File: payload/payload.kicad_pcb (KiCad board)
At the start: 2 copper layers, 90.2 x 95.9 mm, 49 parts, among them IC301 PIC16F1503-I_SL, J101 Conn_02x26_Odd_Even, J102 Conn_02x26_Odd_Even, J301 TC2030-MCP-NL-10, J401 Conn_01x06_Female, J501 Conn_01x02, J502 AVR-ISP-6, U101 PCA9548APW, U401 STM32F103C8T6, U501 ATmega328-P, Y401 8MHz, Y501 ECS-100-S-20A-TR

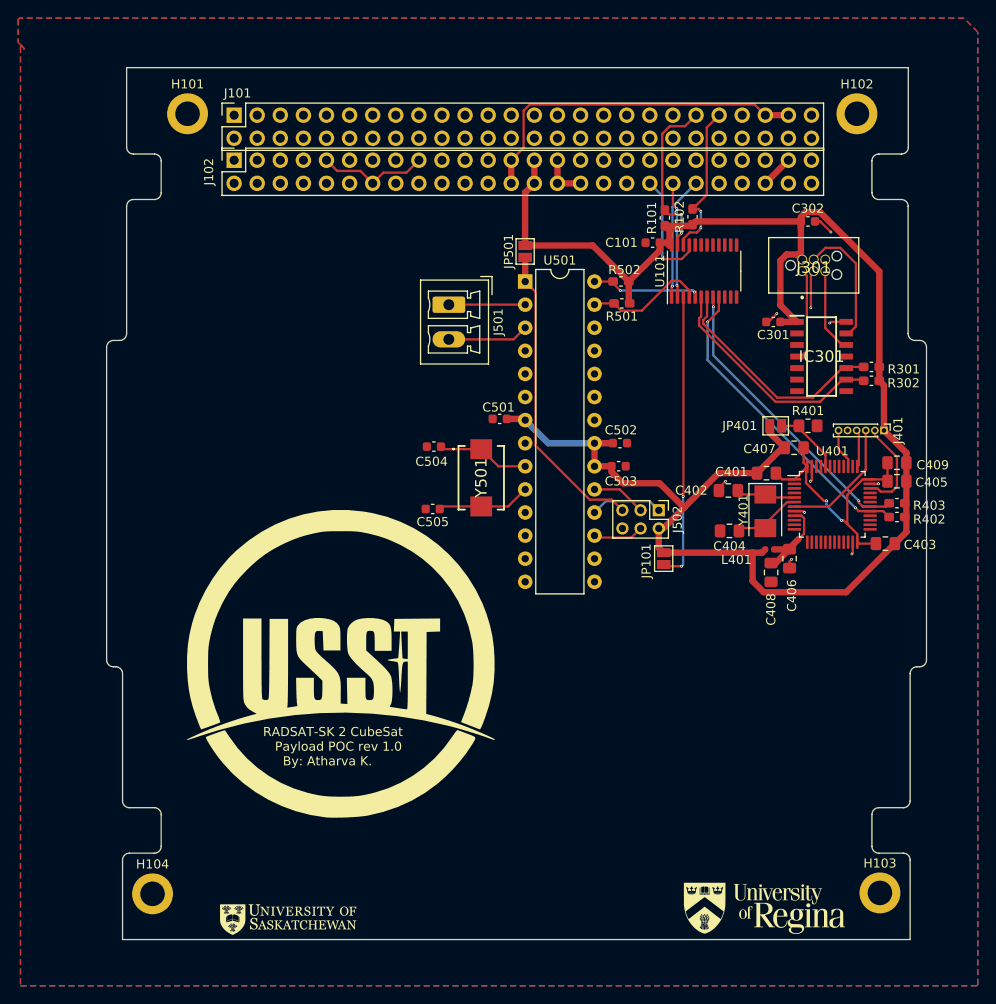
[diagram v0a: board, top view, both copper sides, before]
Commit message: added LEDs
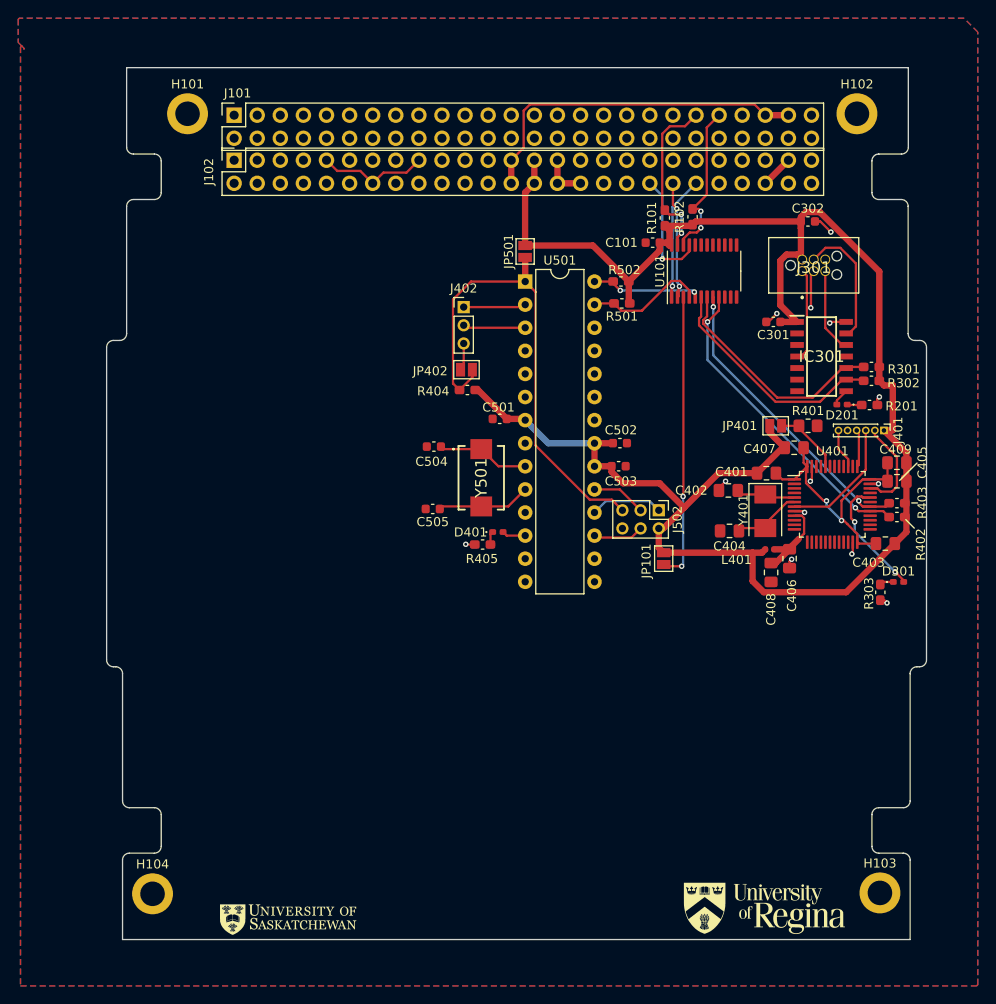
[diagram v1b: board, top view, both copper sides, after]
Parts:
- removed J501: Conn_01x02, Connector_Phoenix_MC:PhoenixContact_MCV_1,5_2-G-3.81_1x02_P3.81mm_Vertical
- added D201: LED, LED_SMD:LED_0402_1005Metric_Pad0.77x0.64mm_HandSolder, F.Cu at (178.1, 85.3)
- added D301: LED, LED_SMD:LED_0402_1005Metric_Pad0.77x0.64mm_HandSolder, F.Cu at (184.3, 104.8)
- added D401: LED, LED_SMD:LED_0402_1005Metric_Pad0.77x0.64mm_HandSolder, F.Cu at (140.3, 99.3)
- added J402: Conn_01x03, Connector_PinHeader_2.00mm:PinHeader_1x03_P2.00mm_Vertical, F.Cu at (136.5, 74.6)
- added JP402: Jumper_2_Open, Jumper:SolderJumper-2_P1.3mm_Open_Pad1.0x1.5mm, F.Cu at (136.8, 81.5)
- added R201: 1k, Capacitor_SMD:C_0603_1608Metric_Pad1.08x0.95mm_HandSolder, F.Cu at (181.1, 85.3)
- added R303: 1k, Capacitor_SMD:C_0603_1608Metric_Pad1.08x0.95mm_HandSolder, F.Cu at (182.3, 105.9)
- added R404: 2k, Capacitor_SMD:C_0603_1608Metric_Pad1.08x0.95mm_HandSolder, F.Cu at (136.9, 83.7)
- added R405: 1k, Capacitor_SMD:C_0603_1608Metric_Pad1.08x0.95mm_HandSolder, F.Cu at (138.6, 100.7)
- G***: moved to B.Cu
- moved G*** 21.2 mm to (141.7, 123.8), turned to 180 degrees
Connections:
- IC301 pad 8: unconnected-(IC301-RC2-Pad8) -> Net-(D201-A)
- U401 pad 32: unconnected-(U401-PA11-Pad32) -> Net-(D301-A)
- U501 pad 12: unconnected-(U501-PD6-Pad12) -> Net-(D401-A)
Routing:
- net Net-(J502-~{RST}): track 33.7 -> 55.5 mm
- net Net-(D301-A): track 0.00 -> 13.5 mm, vias 0 -> 2
- net +3.3V: track 194.5 -> 201.2 mm
- net Net-(J402-Pin_3): track 0.00 -> 3.03 mm
- net GND: track 38.2 -> 41.1 mm, vias 10 -> 13
- net Net-(D401-A): track 0.00 -> 2.60 mm
- net /ATMEL/TXD: track 8.93 -> 6.88 mm
- net Net-(D201-A): track 0.00 -> 1.90 mm
- net Net-(D201-K): track 0.00 -> 1.60 mm
- net Net-(D301-K): track 0.00 -> 1.54 mm
- net /ATMEL/RXD: track 8.40 -> 6.88 mm
- net Net-(D401-K): track 0.00 -> 1.47 mm

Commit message: added TPs
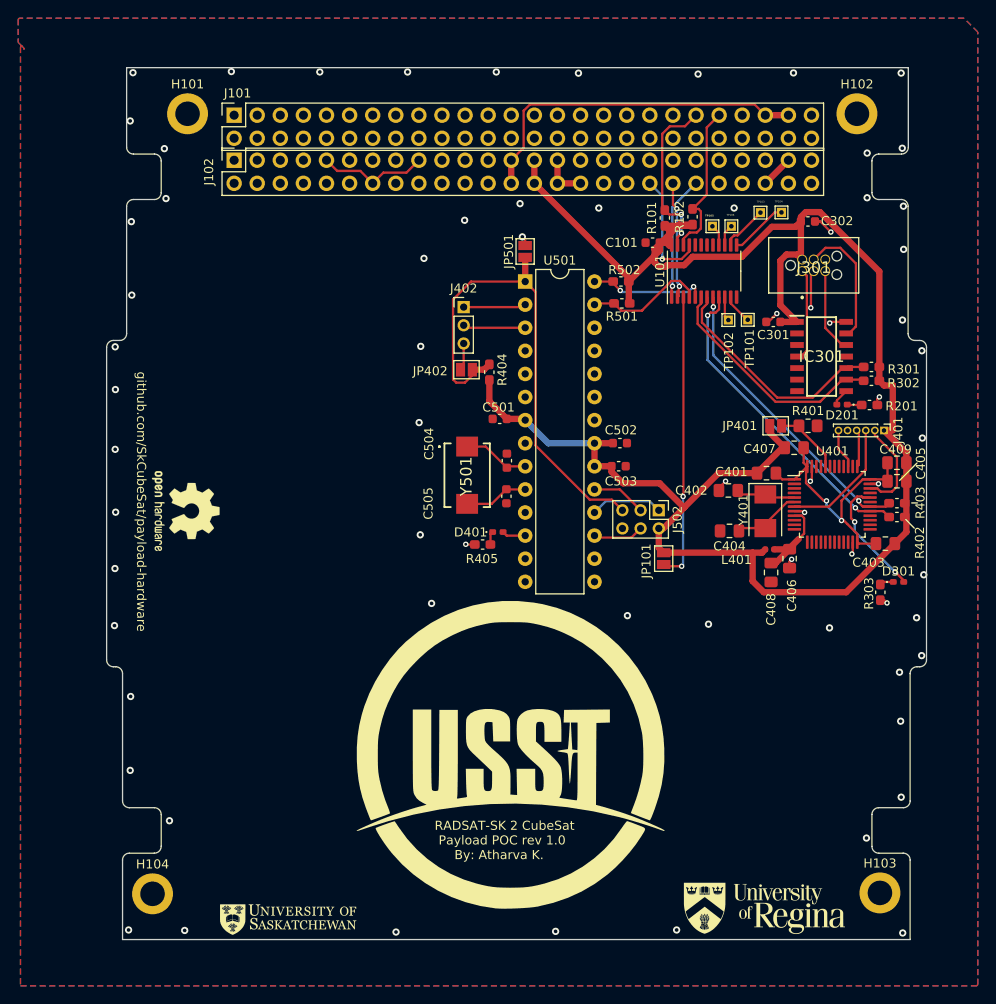
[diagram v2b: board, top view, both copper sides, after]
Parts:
- added REF**: OSHW-Logo2_9.8x8mm_SilkScreen, Symbol:OSHW-Logo2_9.8x8mm_SilkScreen, F.Cu at (105.9, 97.0)
- added TP101: TestPoint, TestPoint:TestPoint_THTPad_1.0x1.0mm_Drill0.5mm, F.Cu at (167.7, 76.0)
- added TP102: TestPoint, TestPoint:TestPoint_THTPad_1.0x1.0mm_Drill0.5mm, F.Cu at (165.6, 76.0)
- added TP103: TestPoint, TestPoint:TestPoint_THTPad_1.0x1.0mm_Drill0.5mm, F.Cu at (169.1, 64.2)
- added TP104: TestPoint, TestPoint:TestPoint_THTPad_1.0x1.0mm_Drill0.5mm, F.Cu at (171.4, 64.2)
- added TP105: TestPoint, TestPoint:TestPoint_THTPad_1.0x1.0mm_Drill0.5mm, F.Cu at (163.9, 65.7)
- added TP106: TestPoint, TestPoint:TestPoint_THTPad_1.0x1.0mm_Drill0.5mm, F.Cu at (165.9, 65.7)
- G***: moved to F.Cu
- R404: value 2k -> 4k7
- moved C505 8.22 mm to (141.2, 95.4), turned to -90 degrees
- moved C504 8.17 mm to (141.2, 91.5), turned to 90 degrees
- moved R404 3.11 mm to (139.3, 81.7), turned to 90 degrees
- moved Y501 1.57 mm to (136.9, 93.1)
- turned G*** to 0 degrees
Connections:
- JP501 pad 2: +3.3V -> GND
- U101 pad 10: unconnected-(U101-SD3-Pad10) -> Net-(U101-SD3)
- U101 pad 11: unconnected-(U101-SC3-Pad11) -> Net-(U101-SC3)
- U101 pad 13: unconnected-(U101-SD4-Pad13) -> Net-(U101-SD4)
- U101 pad 14: unconnected-(U101-SC4-Pad14) -> Net-(U101-SC4)
- U101 pad 15: unconnected-(U101-SD5-Pad15) -> Net-(U101-SD5)
- U101 pad 16: unconnected-(U101-SC5-Pad16) -> Net-(U101-SC5)
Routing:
- net +3.3V: track 201.2 -> 209.3 mm
- net Net-(U101-SD4): track 0.00 -> 6.42 mm
- net Net-(U101-SC4): track 0.00 -> 5.15 mm
- net Net-(U101-SC3): track 0.00 -> 3.31 mm
- net /ATMEL/XTAL2: track 10.3 -> 7.06 mm
- net /ATMEL/XTAL1: track 10.2 -> 7.41 mm
- net Net-(U101-SD3): track 0.00 -> 2.68 mm
- net Net-(U101-SD5): track 0.00 -> 2.36 mm
- net Net-(U101-SC5): track 0.00 -> 2.36 mm
- net /ATMEL/SC0: track 11.6 -> 13.0 mm
- net GND: track 41.1 -> 42.2 mm, vias 13 -> 70
- net Net-(J502-~{RST}): track 55.5 -> 56.5 mm
- net SCL: vias 2 -> 0
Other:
- board text added: "github.com/SkCubeSat/payload-hardware"
